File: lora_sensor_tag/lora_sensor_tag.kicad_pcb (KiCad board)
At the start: 2 copper layers, 123 parts, among them J1 Conn_Coaxial, J2 Conn_Coaxial, J3 Li-ion_bat_conn, J4 USB_C_Receptacle_USB2.0_14P, Q1 NPN, Q2 NPN, Q3 NPN, U1 SX1276IMLTRT, U2 ESP32-WROOM-32D, U3 PE4259, U4 SHT20, U5 TPS63070RNMR, U6 MCP73871-2CAI_ML, U7 AMS1117-3.3, U8 MAX17048G_T10, U9 CP2102N-Axx-xQFN28, Y1 32 MHz

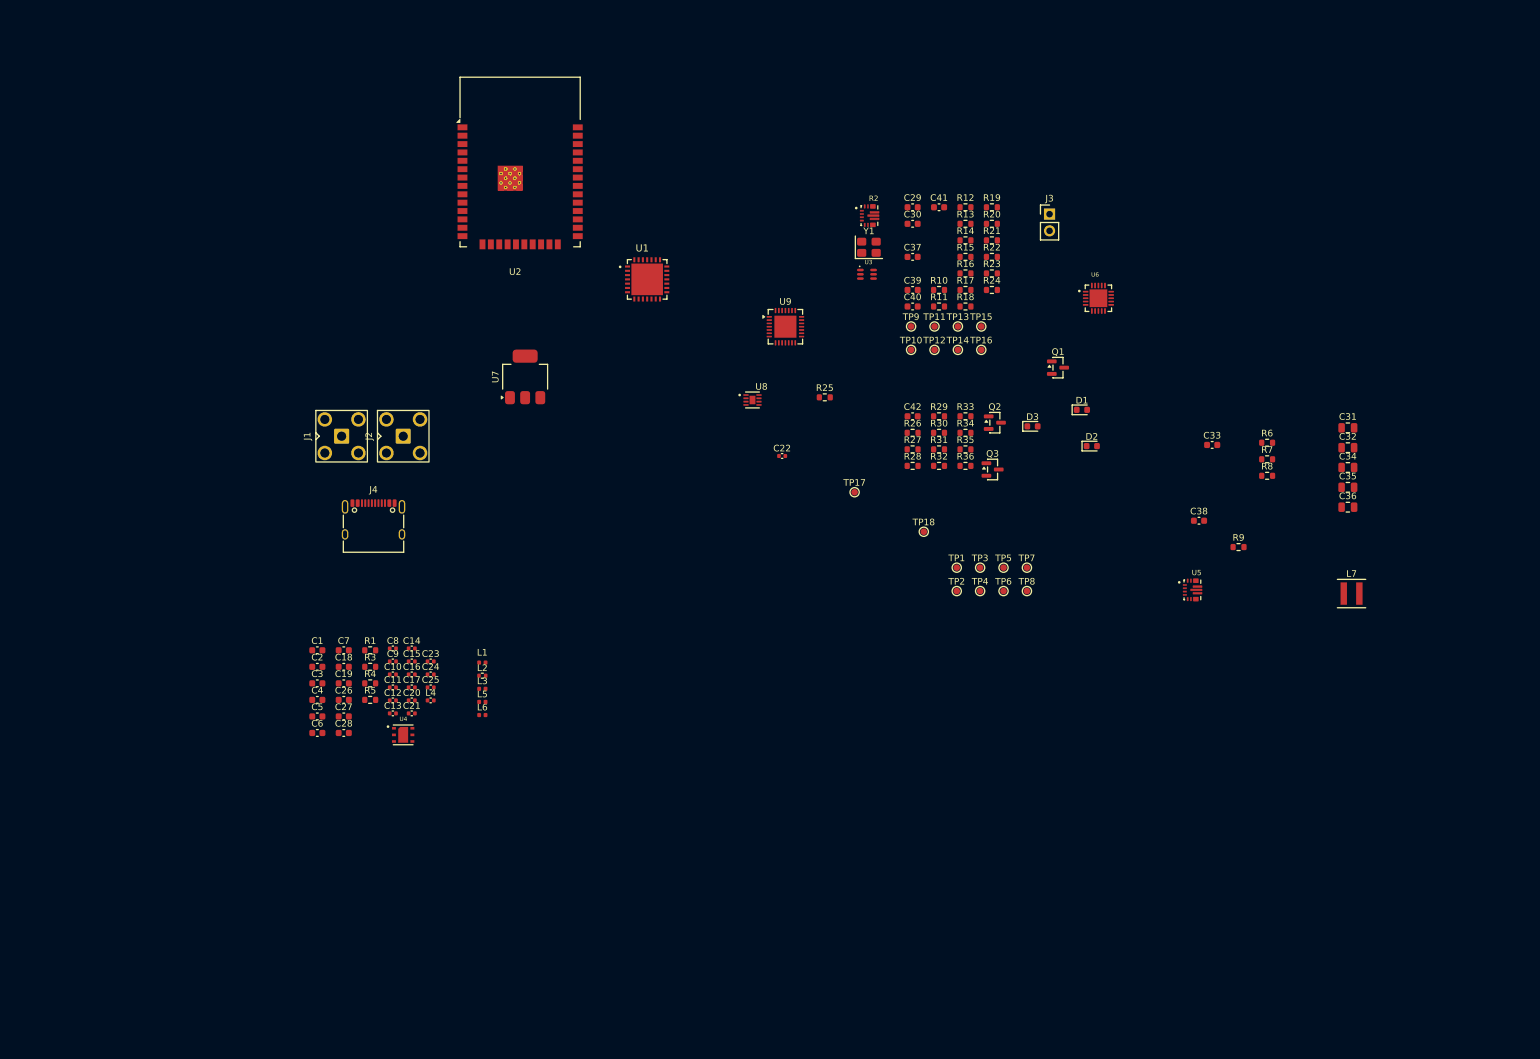
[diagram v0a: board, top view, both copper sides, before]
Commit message: Update schematics
Adds the following updates to the schematics:
- Add power switch to the device;
- Add various LED indicators for device status monitoring;
- Add Reset and Prog buttons for device control;

Signed-off-by: Volodymyr <volodymyrnoha99@gmail.com>
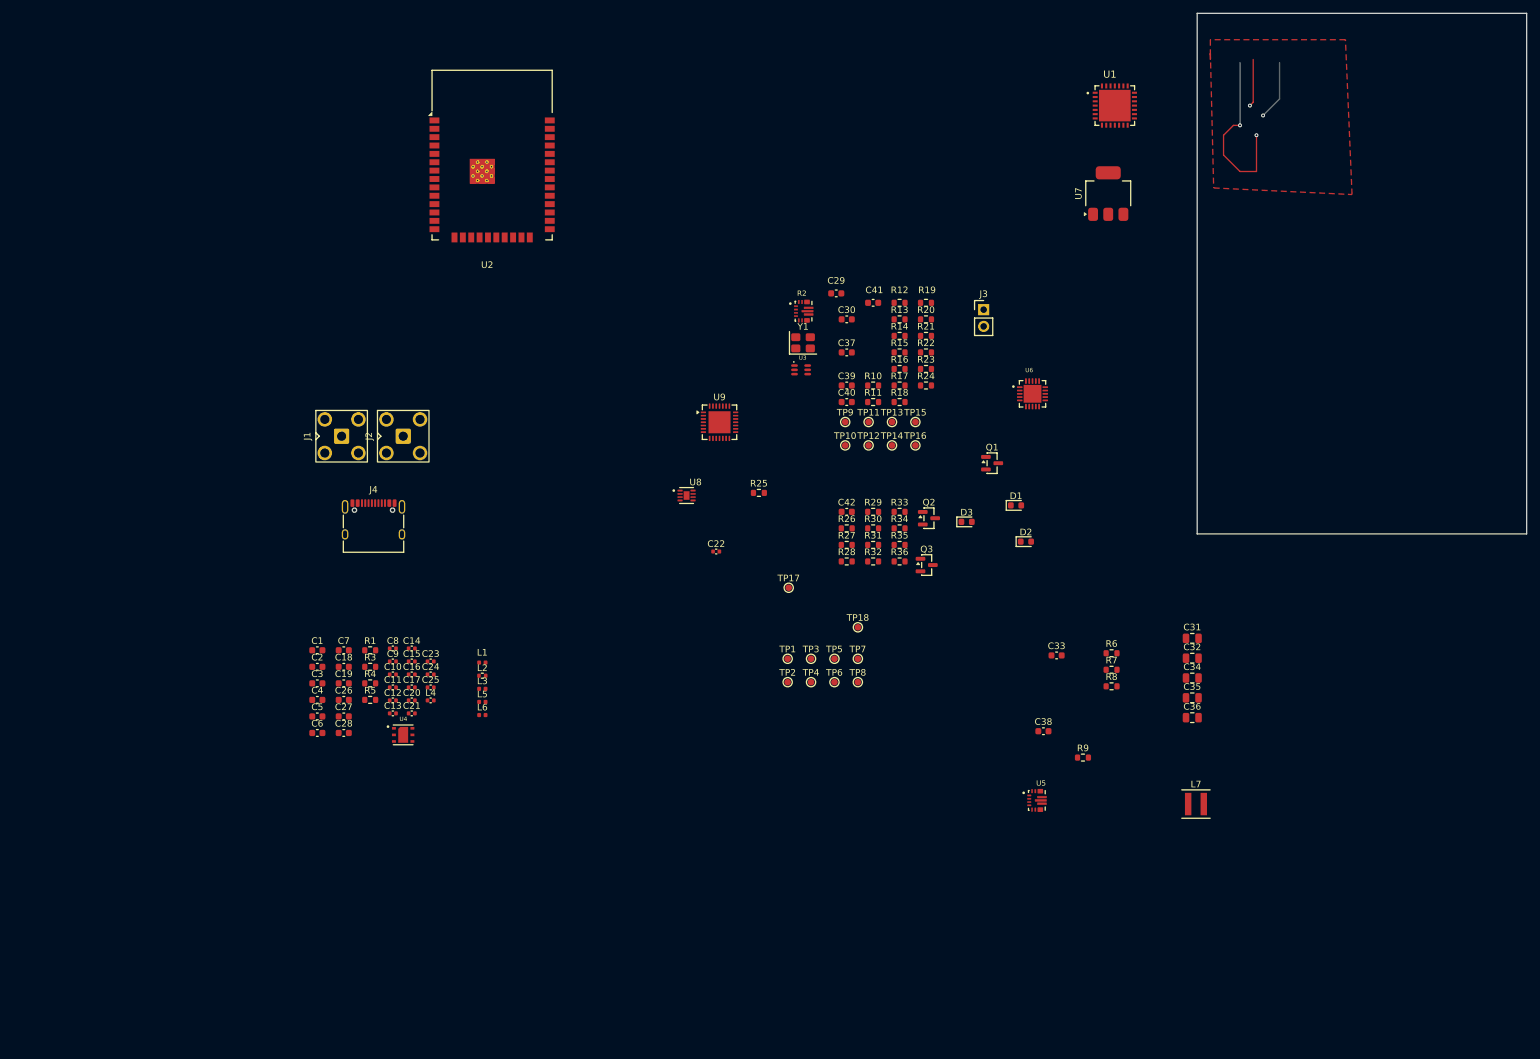
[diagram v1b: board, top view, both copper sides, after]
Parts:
- moved U7 92.8 mm to (186.5, 53.4)
- moved U1 75.7 mm to (187.5, 40.0)
- moved C34 39.7 mm to (199.3, 126.9)
- moved R7 39.7 mm to (187.0, 125.6)
- moved C31 39.7 mm to (199.3, 120.8)
- moved C32 39.7 mm to (199.3, 123.9)
- moved C33 39.7 mm to (178.7, 123.4)
- moved C35 39.7 mm to (199.3, 129.9)
- moved C36 39.7 mm to (199.3, 132.9)
- moved C38 39.7 mm to (176.7, 134.9)
- moved L7 39.7 mm to (199.8, 146.0)
- moved R6 39.7 mm to (187.0, 123.1)
- moved R8 39.7 mm to (187.0, 128.1)
- moved R9 39.7 mm to (182.7, 138.9)
- moved U5 39.7 mm to (175.7, 145.4)
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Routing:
- net (no net): track 0.00 -> 54.8 mm, vias 0 -> 4
- added copper zone on F.Cu, net GND
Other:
- board outline added: 50 x 79 mm
- copper layers 2 -> 4

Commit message: Update PCB routing rules
Signed-off-by: Volodymyr <volodymyrnoha99@gmail.com>
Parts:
- moved J4 8.64 mm to (79.1, 111.6)
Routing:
- net (no net): track 54.8 -> 0.00 mm, vias 4 -> 0
- removed copper zone on F.Cu, net GND
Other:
- board outline removed
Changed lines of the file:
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@@
 	(footprint "Connector_USB:USB_C_Receptacle_XKB_U262-16XN-4BVC11"
 		(layer "F.Cu")
-		(at 75 104)
+		(at 79.11 111.605)
 		(descr "USB Type C, right-angle, SMT, https://datasheet.lcsc.com/szlcsc/1811141824_XKB-Enterprise-U262-161N-4BVC11_C319148.pdf")
 		(tags "USB C Type-C Receptacle SMD")
@@
 			)
 		)
-	)
-	(gr_rect
-		(start 200 26)
-		(end 250 105)
-		(stroke
-			(width 0.05)
-			(type default)
-		)
-		(fill no)
-		(layer "Edge.Cuts")
-	)
-	(segment
-		(start 209 44.5)
-		(end 209 50)
-		(width 0.2)
-		(layer "F.Cu")
-		(net "")
-	)
-	(segment
-		(start 205.5 43)
-		(end 206.5 43)
-		(width 0.2)
-		(layer "F.Cu")
-		(net "")
-	)
-	(segment
-		(start 204 44.5)
-		(end 205.5 43)
-		(width 0.2)
-		(layer "F.Cu")
-		(net "")
-	)
-	(segment
-		(start 206.5 50)
-		(end 204 47.5)
-		(width 0.2)
-		(layer "F.Cu")
-		(net "")
-	)
-	(segment
-		(start 209 50)
-		(end 206.5 50)
-		(width 0.2)
-		(layer "F.Cu")
-		(net "")
-	)
-	(segment
-		(start 208.5 33)
-		(end 208.5 39.5)
-		(width 0.2)
-		(layer "F.Cu")
-		(net "")
-	)
-	(segment
-		(start 204 47.5)
-		(end 204 44.5)
-		(width 0.2)
-		(layer "F.Cu")
-		(net "")
-	)
-	(segment
-		(start 208.5 39.5)
-		(end 208 40)
-		(width 0.2)
-		(layer "F.Cu")
-		(net "")
-	)
-	(via
-		(at 208 40)
-		(size 0.6)
-		(drill 0.3)
-		(layers "F.Cu" "B.Cu")
-		(net "")
-	)
-	(via
-		(at 210 41.5)
-		(size 0.6)
-		(drill 0.3)
-		(layers "F.Cu" "B.Cu")
-		(net "")
-	)
-	(via
-		(at 206.5 43)
-		(size 0.6)
-		(drill 0.3)
-		(layers "F.Cu" "B.Cu")
-		(net "")
-	)
-	(via
-		(at 209 44.5)
-		(size 0.6)
-		(drill 0.3)
-		(layers "F.Cu" "B.Cu")
-		(net "")
-	)
-	(segment
-		(start 212.5 39)
-		(end 210 41.5)
-		(width 0.2)
-		(layer "B.Cu")
-		(net "")
-	)
-	(segment
-		(start 206.5 43)
-		(end 206.5 33.5)
-		(width 0.2)
-		(layer "B.Cu")
-		(net "")
-	)
-	(segment
-		(start 212.5 33.5)
-		(end 212.5 39)
-		(width 0.2)
-		(layer "B.Cu")
-		(net "")
-	)
-	(segment
-		(start 208 40)
-		(end 208 48)
-		(width 0.2)
-		(layer "In1.Cu")
-		(net "")
-	)
-	(segment
-		(start 210 43.5)
-		(end 209 44.5)
-		(width 0.2)
-		(layer "In2.Cu")
-		(net "")
-	)
-	(segment
-		(start 210 41.5)
-		(end 210 43.5)
-		(width 0.2)
-		(layer "In2.Cu")
-		(net "")
-	)
-	(zone
-		(net "GND")
-		(layer "F.Cu")
-		(name "GND_1")
-		(hatch edge 0.5)
-		(connect_pads
-			(clearance 0.5)
-		)
-		(min_thickness 0.25)
-		(fill
-			(thermal_gap 0.5)
-			(thermal_bridge_width 0.5)
-			(island_removal_mode 1)
-		)
-		(polygon
-			(pts
-				(xy 202 32) (xy 202.5 52.5) (xy 223.5 53.5) (xy 222.5 30) (xy 202 30) (xy 202 33)
-			)
-		)

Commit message: pcb_layout: Add initial board layout
Adds:
 - Initial board dimensions;
 - Initial MCU component placement and routing

Signed-off-by: Volodymyr <volodymyrnoha99@gmail.com>
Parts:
- added C23: 1nF, Capacitor_SMD:C_0603_1608Metric, F.Cu at (232.9, 74.7)
- added C24: 1nF, Capacitor_SMD:C_0603_1608Metric, F.Cu at (233.2, 58.6)
- added D1: MCU_ST, LED_SMD:LED_0603_1608Metric, F.Cu at (201.9, 41.6)
- added H1: MountingHole_Pad, MountingHole:MountingHole_2.7mm_M2.5_Pad_Via, F.Cu at (169.5, 95.1)
- added H2: MountingHole_Pad, MountingHole:MountingHole_2.7mm_M2.5_Pad_Via, F.Cu at (231.6, 95.5)
- added H3: MountingHole_Pad, MountingHole:MountingHole_2.7mm_M2.5_Pad_Via, F.Cu at (170.0, 129.5)
- added H4: MountingHole_Pad, MountingHole:MountingHole_2.7mm_M2.5_Pad_Via, F.Cu at (231.0, 129.5)
- added R23: 470R, Resistor_SMD:R_0603_1608Metric, F.Cu at (121.5, 64.8)
- added R27: 470R, Resistor_SMD:R_0603_1608Metric, F.Cu at (121.5, 67.3)
- added R30: 470R, Resistor_SMD:R_0603_1608Metric, F.Cu at (121.5, 69.8)
- added R31: 470R, Resistor_SMD:R_0603_1608Metric, F.Cu at (121.5, 72.3)
- added R42: 470R, Resistor_SMD:R_0603_1608Metric, F.Cu at (121.5, 76.8)
- added R45: 470R, Resistor_SMD:R_0603_1608Metric, F.Cu at (121.5, 79.3)
- added R5: 470R, Resistor_SMD:R_0603_1608Metric, F.Cu at (203.6, 41.6)
- added R6: 470R, Resistor_SMD:R_0603_1608Metric, F.Cu at (231.3, 74.7)
- added R7: 470R, Resistor_SMD:R_0603_1608Metric, F.Cu at (231.7, 58.6)
- added SW1: SW_MCU_RST, Button_Switch_SMD:SW_Push_1TS009xxxx-xxxx-xxxx_6x6x5mm, F.Cu at (231.3, 80.7)
- added SW2: SW_MCU_PROG, Button_Switch_SMD:SW_Push_1TS009xxxx-xxxx-xxxx_6x6x5mm, F.Cu at (231.7, 64.7)
- added SW_PWR1: SW_Nidec_CAS-120A1, Button_Switch_SMD:Nidec_Copal_CAS-120A, F.Cu at (126.3, 67.0)
- R13: renamed from R10; value R -> 0R
- R14: renamed from R11; value R -> 0R
- R15: renamed from R12; value R -> 0R
- R16: renamed from R13; value R -> 0R
- R17: renamed from R14; value R -> 0R
- R18: renamed from R15; value R -> 0R
- R2: footprint TPS63070RNMR:VREG_TPS63070RNMR -> Resistor_SMD:R_0603_1608Metric
- moved R3 176.2 mm to (231.1, 44.5), turned to 90 degrees
- moved R4 175.6 mm to (231.1, 48.3), turned to 90 degrees
- moved C1 163.5 mm to (208.5, 41.6), turned to 90 degrees
- moved C2 163.1 mm to (206.5, 41.6), turned to 90 degrees
- moved C3 162.8 mm to (207.4, 46.2), turned to 180 degrees
- moved R1 154.2 mm to (207.4, 44.4)
- moved U2 126.6 mm to (219.6, 49.3)
- moved J1 124.3 mm to (182.9, 38.0)
- moved J4 123.6 mm to (201.3, 129.8)
- moved U1 114.6 mm to (82.5, 86.0)
- moved J2 106.6 mm to (172.4, 38.0)
- moved U7 94.7 mm to (98.0, 87.0)
- moved U9 82.2 mm to (47.1, 105.0), turned to 90 degrees
- moved R2 63.4 mm to (85.5, 103.0)
- moved TP17 61.3 mm to (91.0, 152.5)
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- renumbered C23 to C25, C24 to C26, C25 to C27, C26 to C28, C27 to C29, C28 to C30, C29 to C31, C30 to C32, C31 to C33, C32 to C34, C33 to C35, C34 to C36, C35 to C37, C36 to C38, C37 to C39, C38 to C40, C39 to C41, C40 to C42, C41 to C43, C42 to C44, D1 to D6, D2 to D7, D3 to D8, R7 to R10, R8 to R11, R9 to R12, R16 to R19, R17 to R20, R18 to R21, R19 to R22, R20 to R24, R21 to R25, R22 to R26, R23 to R28, R24 to R29, R25 to R32, R26 to R33, R27 to R34, R28 to R35, R29 to R36, R30 to R37, R31 to R38, R32 to R39, R33 to R40, R34 to R41, R35 to R43, R36 to R44, R5 to R8, R6 to R9
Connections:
- net /MCU_main_part/MCU_RX renamed /usb_and_prog/RX
- net /MCU_main_part/MCU_TX renamed /usb_and_prog/TX
- J3 pad 1: VBAT -> Net-(J3-Pin_1)
- U2 pad 11: unconnected-(U2-IO26-Pad11) -> /MCU_main_part/MCU_ST
- U6 pad 6: unconnected-(U6-~{PG}-Pad6) -> /power/PG
- U6 pad 7: unconnected-(U6-STAT2-Pad7) -> /power/STAT2
- U6 pad 8: unconnected-(U6-STAT1/~{LBO}-Pad8) -> /power/STAT1\LBO
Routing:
- net /MCU_main_part/MCU_EN: track 0.00 -> 54.8 mm, vias 0 -> 2
- net /usb_and_prog/TX: track 0.00 -> 20.8 mm
- net /usb_and_prog/RX: track 0.00 -> 19.2 mm
- net /MCU_main_part/MCU_ST: track 0.00 -> 18.4 mm, vias 0 -> 2
- net GND: track 0.00 -> 11.6 mm, vias 0 -> 6
- net 3V3: track 0.00 -> 6.99 mm
- net Net-(C24-Pad2): track 0.00 -> 3.96 mm
- net Net-(C23-Pad2): track 0.00 -> 3.77 mm
- net /MCU_main_part/MCU_IO0: track 0.00 -> 3.39 mm
- net /MCU_main_part/SCL: track 0.00 -> 2.79 mm
- net /MCU_main_part/SDA: track 0.00 -> 2.78 mm
- net Net-(D1-A): track 0.00 -> 1.71 mm
- added copper zone on B.Cu, net GND
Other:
- board outline added: 70 x 100 mm
- board text added: "MCU_ST"
- board text added: "PROG"
- board text added: "RST"
- board text added: "loRa"
